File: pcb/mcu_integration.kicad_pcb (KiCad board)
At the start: 4 copper layers, 90.2 x 95.9 mm, 103 parts, among them IC1 TL7660IDGKR, IC10 AD844_OPAMP_MEL, IC3 FOD814_OPTO_NOSHD, IC5 FOD814_OPTO_MEL, IC6 AD844_OPAMP_AL, IC7 FOD814_OPTO_AL, IC8 AD844_OPAMP_NOSHD, IC9 TL081IDT, J4 Conn_01x02, J5 DM3BT-DSF-PEJS, M1 MountingHole_Pad, M2 MountingHole_Pad, M3 MountingHole_Pad, M4 MountingHole_Pad, U1 STM32F103RBTx, U2 REF192_NOSHD, U3 REF192_AL, U4 REF192_MEL, U5 TPS2069CDBVR_MOSFET, U6 LM35DM

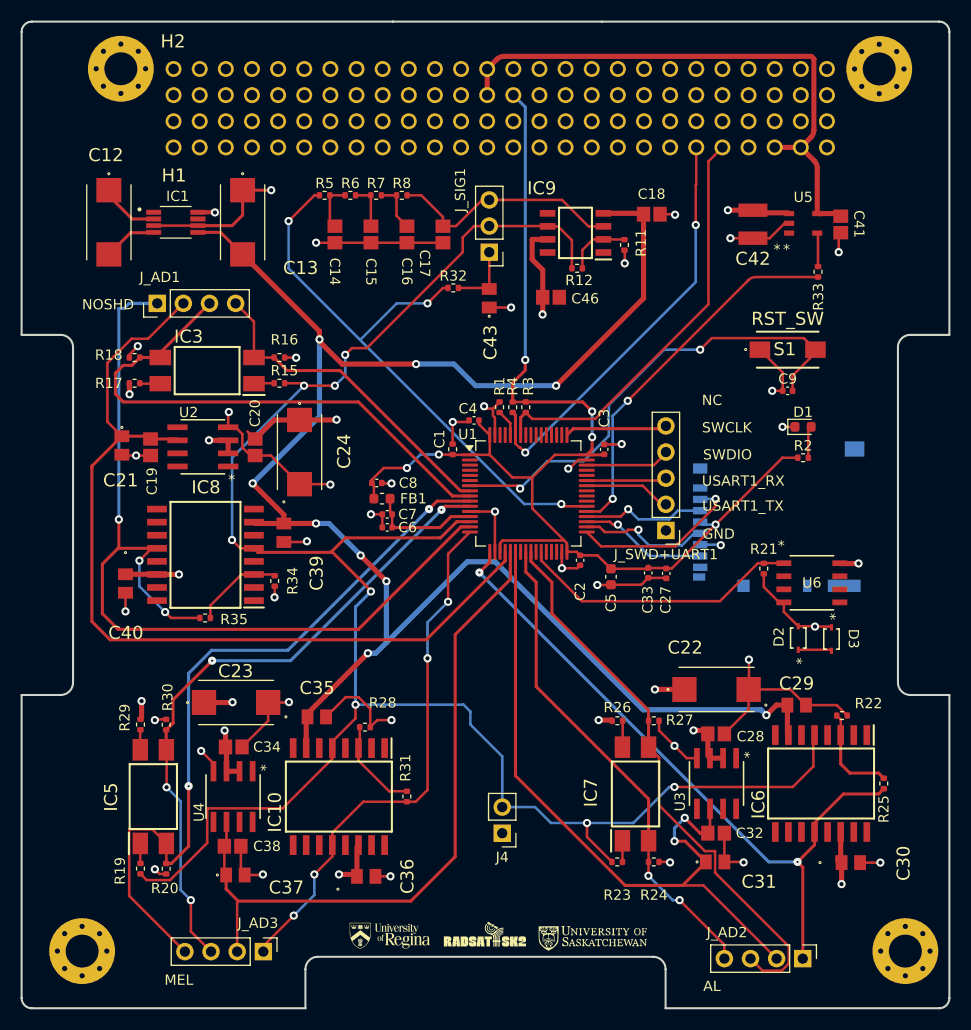
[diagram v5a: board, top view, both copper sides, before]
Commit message: Fixed silkscreen and component values
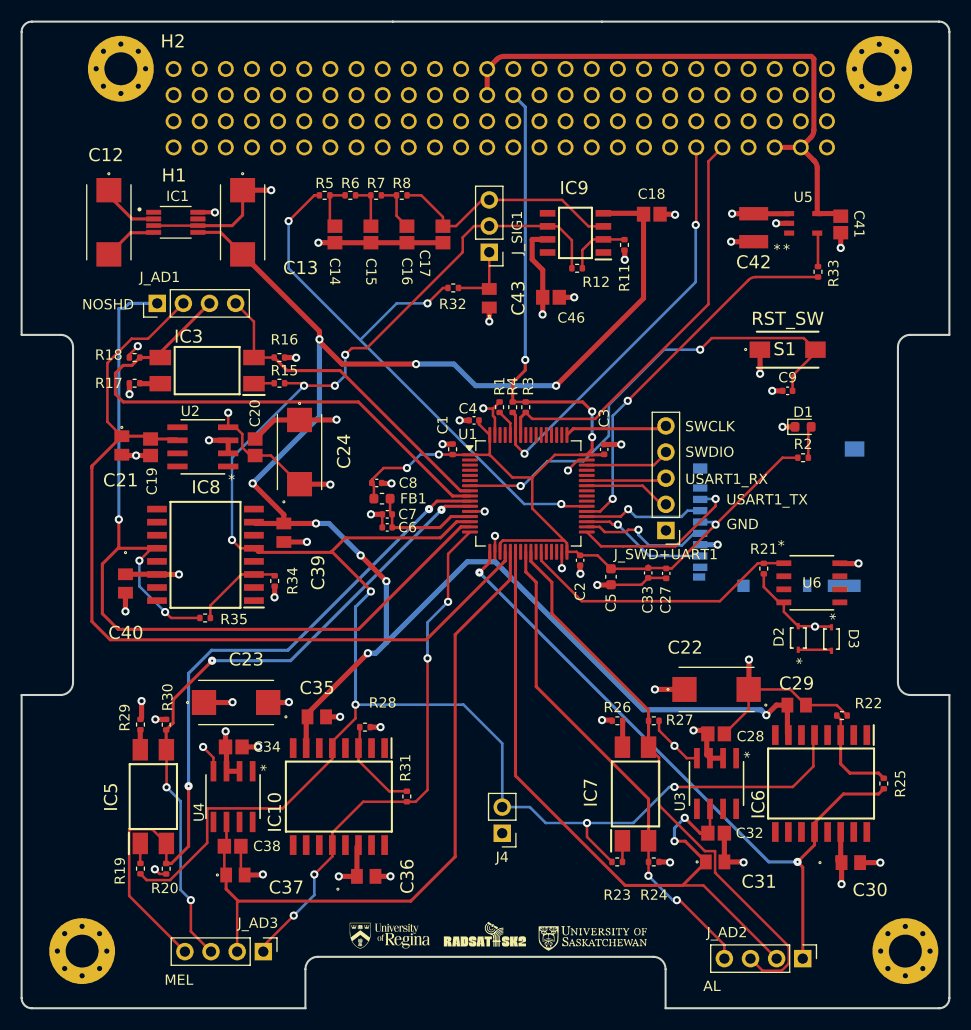
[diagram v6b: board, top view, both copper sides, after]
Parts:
- C14, C15, C16, C17: value 0.01u -> 0.47u
- R5, R6, R7, R8: value 100K -> 3.3K
- moved C42 0.35 mm to (163.7, 71.6)
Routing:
- net GND: track 182.0 -> 158.8 mm, vias 40 -> 48
- net +5V: track 69.9 -> 68.0 mm
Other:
- board text added: "CUBICS Analog IC Shielding Payload REV D Hunter Gerbrandt, Owen Markewich"
- board text removed: "CUBICS Analog IC Shielding Payload REV C Hunter Gerbrandt, Owen Markewich"
- board text removed: "NC"

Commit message: Updated CSKB connector
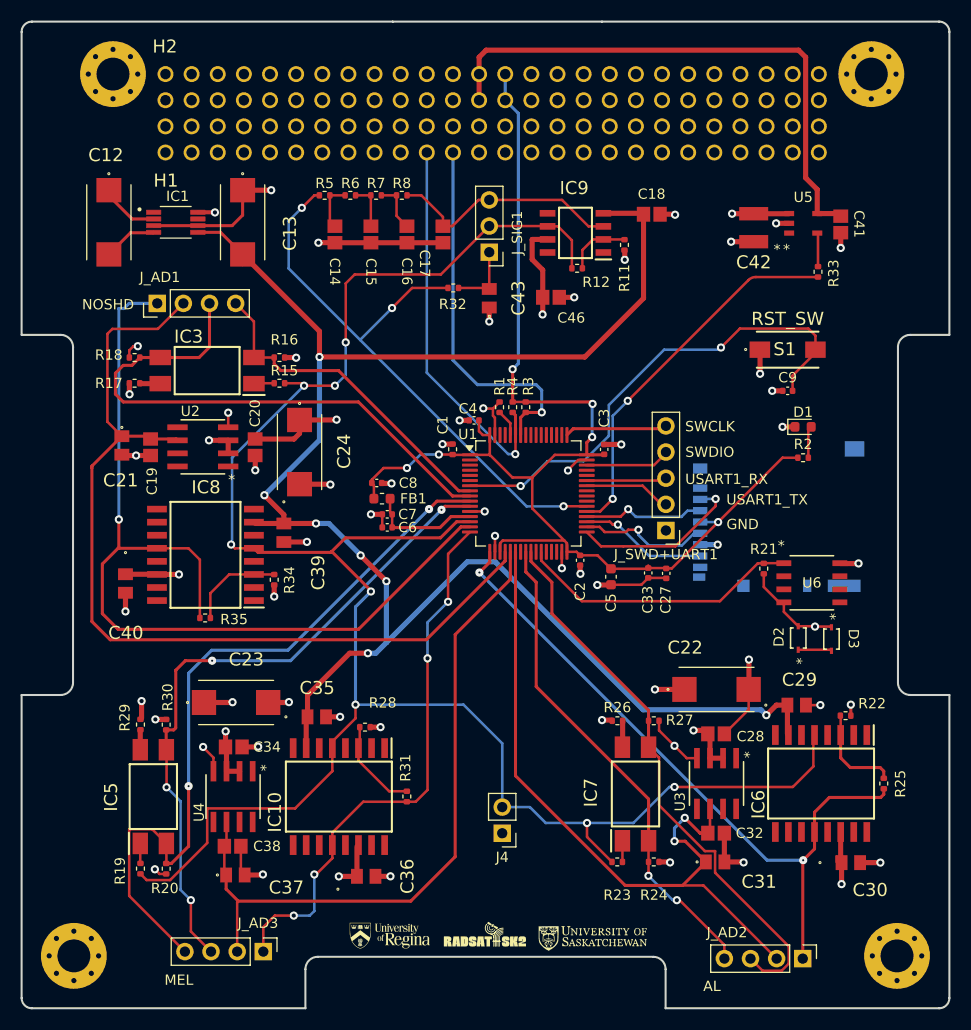
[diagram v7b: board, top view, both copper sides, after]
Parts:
- moved M3 0.94 mm to (177.6, 142.4)
- moved H1 0.93 mm to (106.5, 64.3)
- moved H2 0.93 mm to (106.5, 59.3)
- moved M4 0.93 mm to (97.6, 142.4)
- moved M1 0.92 mm to (101.4, 56.7)
- moved M2 0.91 mm to (175.1, 56.7)
- moved R22 0.35 mm to (172.6, 119.1)
- moved R34 0.13 mm to (117.1, 105.9)
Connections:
- H1 pad 21: unconnected-(H1-Pad21) -> OBC_I2C_SDA
- H1 pad 23: unconnected-(H1-Pad23) -> OBC_I2C_SCL
- H1 pad 41: OBC_I2C_SDA -> unconnected-(H1-Pad41)
- H1 pad 43: OBC_I2C_SCL -> unconnected-(H1-Pad43)
- H1 pad 47: +5V_EXT -> unconnected-(H1-Pad47)
- H1 pad 49: +5V_EXT -> unconnected-(H1-Pad49)
- H2 pad 28: unconnected-(H2-Pad28) -> 3.3V Output
- H2 pad 47: GND -> unconnected-(H2-Pad47)
- H2 pad 48: GND -> unconnected-(H2-Pad48)
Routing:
- net GND: track 158.8 -> 141.9 mm, vias 48 -> 51
- net OBC_I2C_SCL: track 40.9 -> 36.1 mm, vias 0 -> 1
- net ADC1_IN0_SINE: track 194.6 -> 198.9 mm
- net OBC_I2C_SDA: track 41.2 -> 37.5 mm, vias 2 -> 1
- net -5V Output: track 175.6 -> 172.4 mm, vias 9 -> 7
- net 3.3V Output: track 120.2 -> 123.1 mm
- net ADC1_IN11_OPTO_E_NOSHD: track 52.8 -> 55.0 mm
- net ADC1_IN2_OPAMP_MEL: track 52.1 -> 54.2 mm
- net ADC1_IN13_OPTO_E_MEL: track 63.2 -> 65.2 mm
- net +5V_EXT: track 56.3 -> 54.6 mm
- net ADC1_IN4_VREF_NOSHD: track 87.9 -> 89.6 mm
- net /NRST: track 46.7 -> 48.3 mm
- net ADC1_IN1_OPAMP_NOSHD: track 90.3 -> 89.3 mm, vias 3 -> 1
- net +5V: track 68.0 -> 69.0 mm
- net ADC1_IN3_OPAMP_AL: track 67.8 -> 68.8 mm
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
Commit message: Added missing decoupling capacitor + changed capacitors footprint
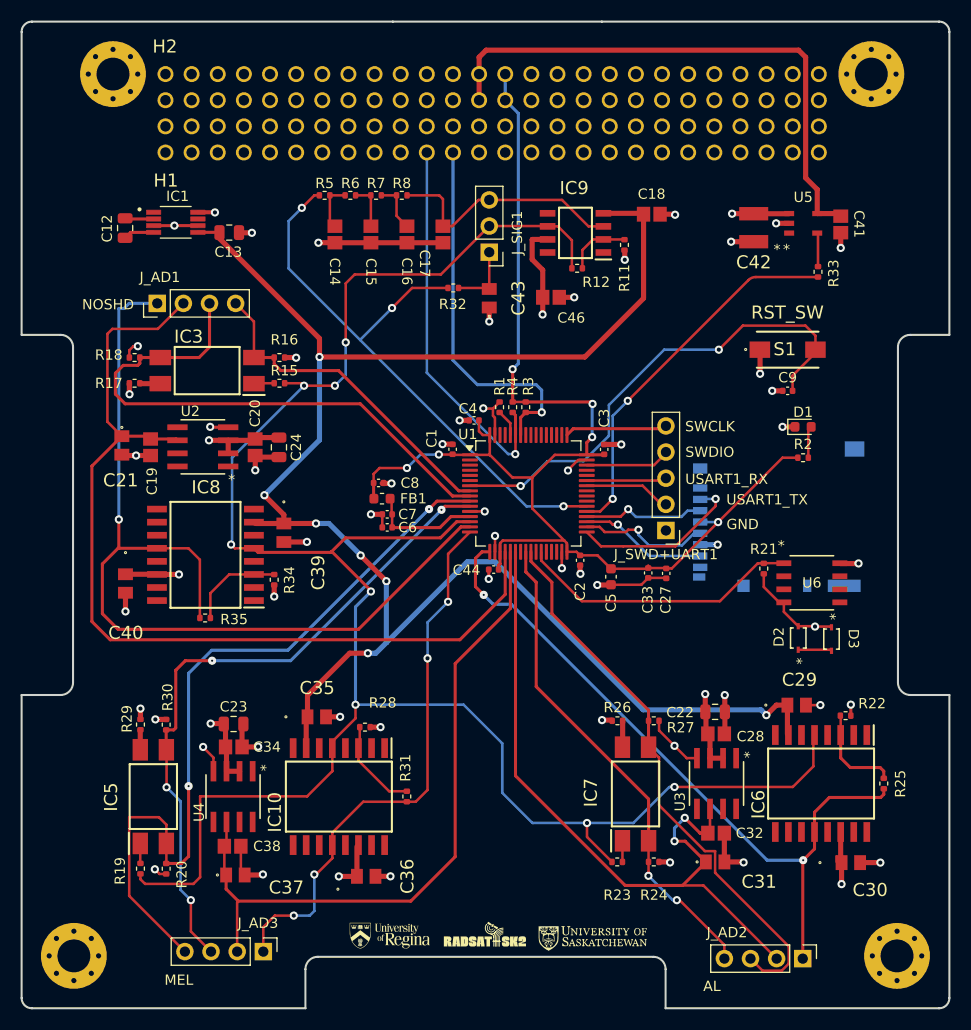
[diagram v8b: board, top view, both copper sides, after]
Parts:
- removed J4: Conn_01x02, Connector_PinHeader_2.54mm:PinHeader_1x02_P2.54mm_Vertical
- added C44: 100n, Capacitor_SMD:C_0402_1005Metric, F.Cu at (138.4, 104.9)
- C1: footprint Resistor_SMD:R_0402_1005Metric -> Capacitor_SMD:C_0402_1005Metric
- C12, C13, C22, C23, C24: footprint capstone:T495D -> Capacitor_SMD:C_0805_2012Metric
- moved C22 2.18 mm to (159.9, 118.7)
- moved C23 2.10 mm to (113.2, 119.9)
- moved C24 2.05 mm to (117.6, 93.0)
- moved C12 1.68 mm to (102.6, 71.7)
- moved C13 1.64 mm to (112.7, 72.1), turned to 180 degrees
- moved C8 0.17 mm to (127.2, 96.5)
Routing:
- net GND: track 141.9 -> 129.4 mm
- net +5V: track 69.0 -> 62.8 mm, vias 16 -> 13
- net ADC1_IN12_OPTO_F_MEL: track 74.2 -> 77.5 mm
- net Net-(C12-+): track 5.82 -> 2.80 mm
- net ADC1_IN0_SINE: track 198.9 -> 201.3 mm
- net Net-(C12--): track 5.24 -> 2.99 mm
- net ADC1_IN4_VREF_NOSHD: track 89.6 -> 91.5 mm
- net 3.3V Output: track 123.1 -> 124.9 mm
- net ADC1_IN3_OPAMP_AL: track 68.8 -> 70.6 mm
- net -5V Output: track 172.4 -> 171.4 mm
- net RC_OUTPUT: track 23.0 -> 24.0 mm
